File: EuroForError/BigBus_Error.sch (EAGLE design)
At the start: 47 parts

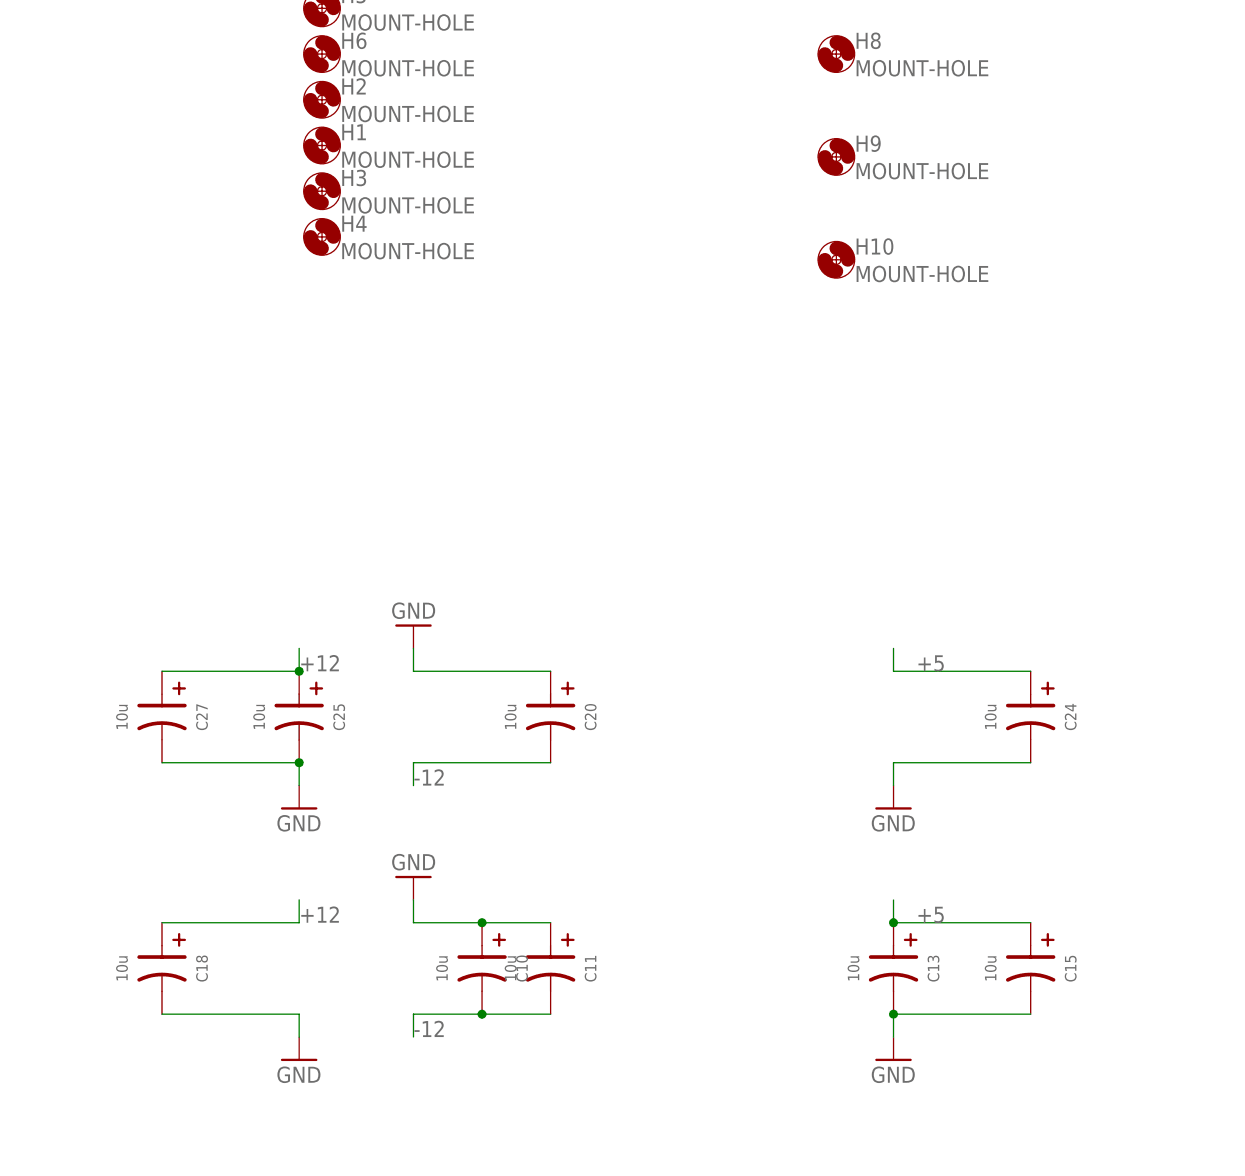
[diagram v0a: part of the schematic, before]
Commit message: BigBus - Tuesday tracenames for calibration-fixups, Finaleffect/flask routed
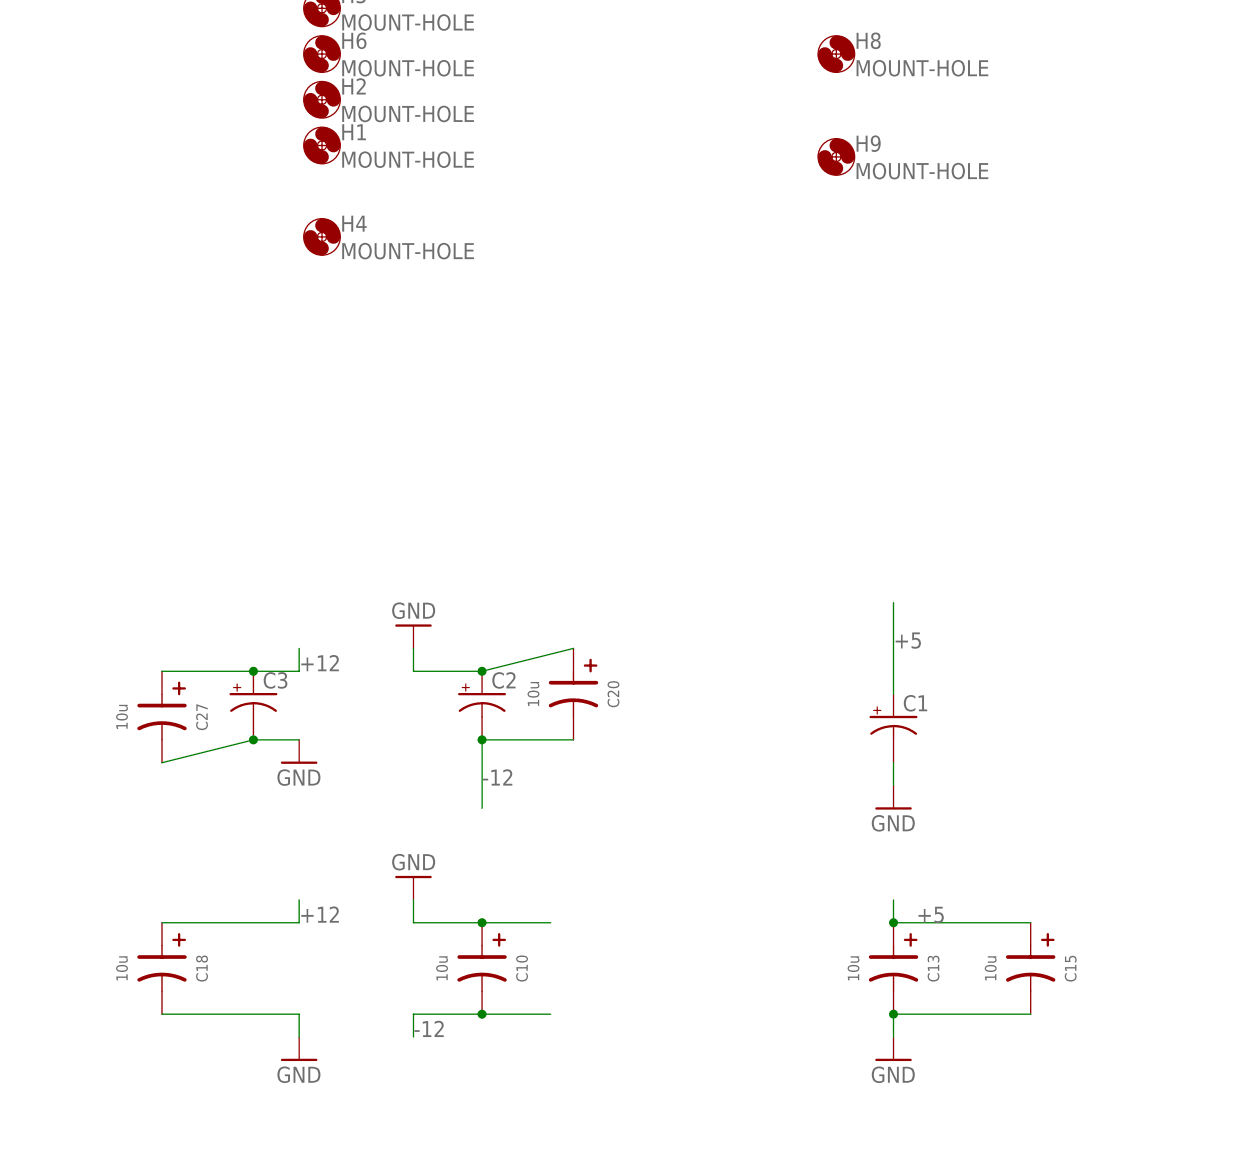
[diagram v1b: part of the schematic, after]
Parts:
- removed C11, C24, C25: 10u, EurorackModularParts:C-POLAR-A
- removed H10, H3: MOUNT-HOLE, zephod-components:MOUNT-HOLE
- added C1, C2, C3: (no value), SparkFun-Capacitors:CAP_POLD
- U$1, U$10, U$11, U$12, U$13, U$14, U$15, U$16, U$17, U$20, U$3, U$4, U$5, U$6, U$8, U$9: value POWERSHROUDED -> POWER_SHROUDED_NOTEXT; device EurorackModularParts:POWERSHROUDED -> EurorackModularParts:POWER_SHROUDED_NOTEXT
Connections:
- net +12: now also C3.+; no longer C25.1
- net +5: now also C1.+; no longer C24.1
- net -12: now also C2.-; no longer C11.2
- net GND: now also C1.-, C2.+, C3.-; no longer C11.1, C24.2, C25.2
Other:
- moved on the sheet: C20

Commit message: Perplexed, PowerBus, Wobbler/Edgecutter/Tuesday updates, FinalEffect
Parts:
- C1, C2, C3: value (none) -> 10uF
- C10, C13, C15, C18, C20, C27: value 10u -> 10uF
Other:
- moved on the sheet: U$10
